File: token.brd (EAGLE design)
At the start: 25 x 25 mm, 9 parts

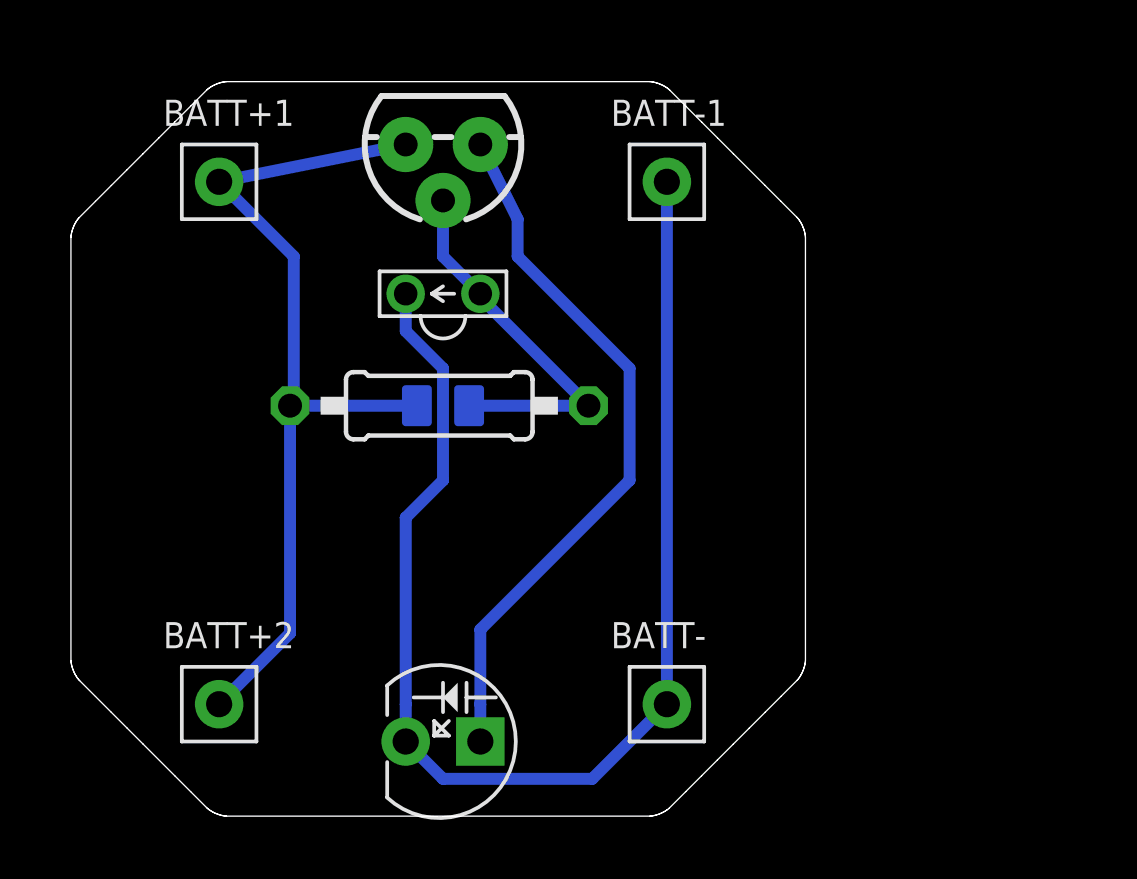
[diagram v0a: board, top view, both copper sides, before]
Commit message: Rearranged parts, updated routing
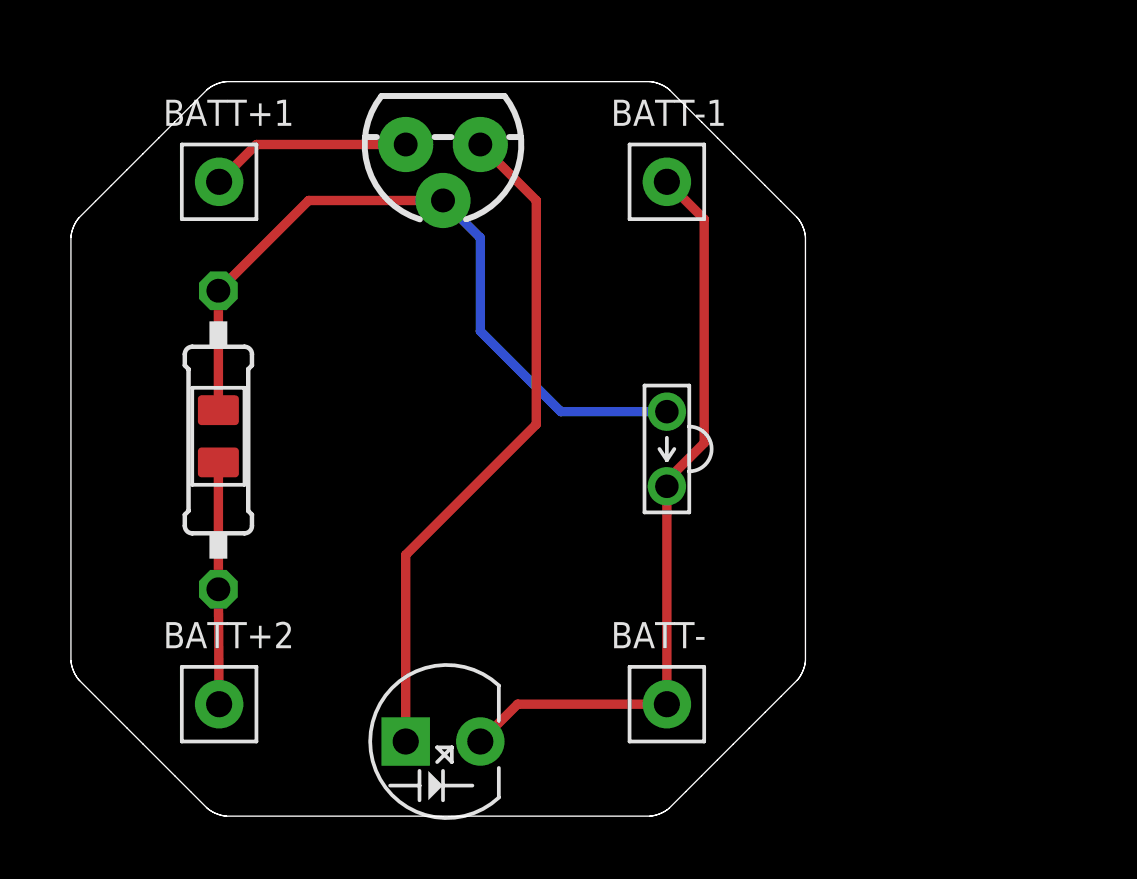
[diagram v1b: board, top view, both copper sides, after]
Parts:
- moved LTR-4206E 9.27 mm to (20.3, 12.5), turned to 90 degrees
- moved R1 7.72 mm to (5.05, 12.9), turned to 270 degrees
- moved R1-ALT 7.72 mm to (5.05, 12.9), flipped to the top, turned to 0 degrees
- turned LED to 0 degrees
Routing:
- net GND: track 44.5 -> 25.7 mm
- net VCC: track 30.7 -> 15.1 mm
- net N$2: track 13.1 -> 25.4 mm
- net N$1: track 24.3 -> 23.0 mm

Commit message: Added PCB art
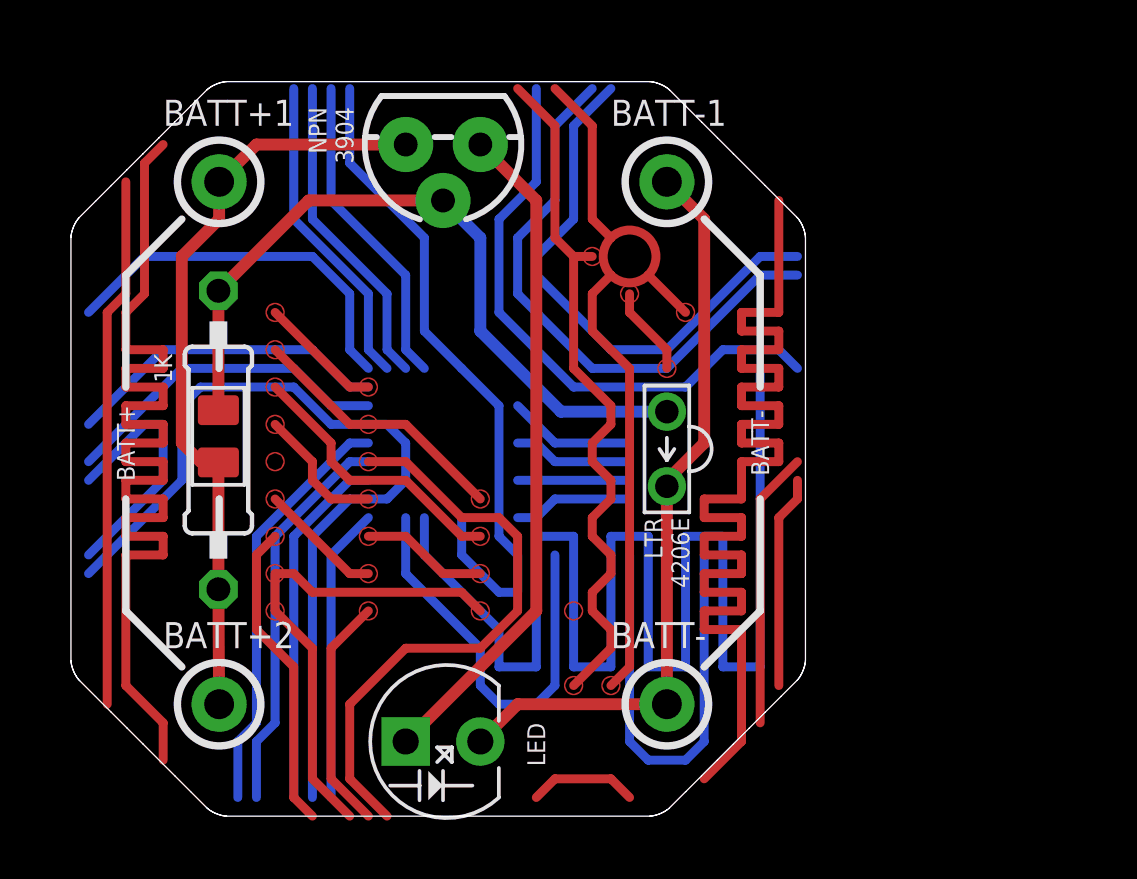
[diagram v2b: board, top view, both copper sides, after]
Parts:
- BATT+1, BATT+2, BATT-, BATT-1: device Seeed-OPL-Connector:1P-65/35MIL -> SparkFun-Connectors:1X01NS-KIT
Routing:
- net N$26: track 0.00 -> 51.9 mm
- net N$62: track 0.00 -> 41.8 mm
- net N$60: track 0.00 -> 37.2 mm
- net N$37: track 0.00 -> 29.8 mm
- net N$59: track 0.00 -> 24.4 mm
- net N$38: track 0.00 -> 20.1 mm
- net N$55: track 0.00 -> 20.0 mm
- net N$39: track 0.00 -> 19.9 mm
- net N$40: track 0.00 -> 18.7 mm
- net N$61: track 0.00 -> 18.0 mm
- net N$52: track 0.00 -> 16.8 mm
- net N$41: track 0.00 -> 15.8 mm
- net N$57: track 0.00 -> 15.0 mm
- net N$42: track 0.00 -> 14.3 mm
- net N$29: track 0.00 -> 14.3 mm
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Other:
- board text added: "1K"
- board text added: "BATT+"
- board text added: "BATT-"
- board text added: "LED"
- board text added: "LTR 4206E"
- board text added: "NPN 3904"

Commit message: Initial wiring and routing
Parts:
- removed BATT+1, BATT+2, BATT-, BATT-1: 1p-2.54, SparkFun-Connectors:1X01NS-KIT
- removed LTR-4206E: (no value), SparkFun-Sensors:LTR-301
- removed Q1: (no value), SparkFun-DiscreteSemi:TO-92
- removed R1: 1K, Seeed-OPL-Resistor:PR-D2.3XL6.5MM
- removed R1-ALT: 1K, Seeed-OPL-Resistor:R0805
- added D1, D2, D3, D4, D6, D7, D8: (no value), adafruit:LED2X5
- turned LED to 180 degrees
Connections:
- removed net GND: BATT-.1, BATT-1.1, LED.-, LTR-4206E.E
- removed net VCC: BATT+1.1, BATT+2.1, Q1.3, R1-ALT.2, R1.2
- new net N$45: D2.K, D3.A
- new net N$48: D3.K, D4.A
- new net N$51: D4.K, LED.+
- new net N$54: D6.A, LED.-
- new net N$59: D6.K, D7.A
- new net N$65: D7.K, D8.A
- net N$1: now also D1.A, D8.K; no longer LED.+, Q1.1
- net N$2: now also D1.K, D2.A; no longer LTR-4206E.C, Q1.2, R1-ALT.1, R1.1
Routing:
- net N$65: track 0.00 -> 107.4 mm, vias 0 -> 1
- net N$51: track 4.23 -> 107.1 mm, vias 0 -> 1
- net N$45: track 4.23 -> 107.1 mm, vias 0 -> 1
- net N$48: track 4.60 -> 107.3 mm, vias 0 -> 1
- net N$54: track 9.09 -> 107.1 mm, vias 0 -> 1
- net N$1: track 23.0 -> 107.4 mm, vias 0 -> 1
- net N$59: track 24.4 -> 107.2 mm, vias 0 -> 1
- net N$2: track 25.4 -> 107.0 mm, vias 0 -> 1
- net N$26: track 51.9 -> 0.00 mm
- net N$62: track 41.8 -> 0.00 mm
- net N$60: track 37.2 -> 0.00 mm
- net N$37: track 29.8 -> 0.00 mm
- net VCC: track 26.0 -> 0.00 mm
- net GND: track 25.7 -> 0.00 mm
- net N$38: track 20.1 -> 0.00 mm
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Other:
- board text removed: "1K"
- board text removed: "BATT-"
- board text removed: "LTR 4206E"
- board text removed: "NPN 3904"
